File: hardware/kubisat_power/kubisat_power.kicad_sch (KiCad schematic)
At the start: 21 parts, among them U1 TPS79601DCQ, U2 INA3221

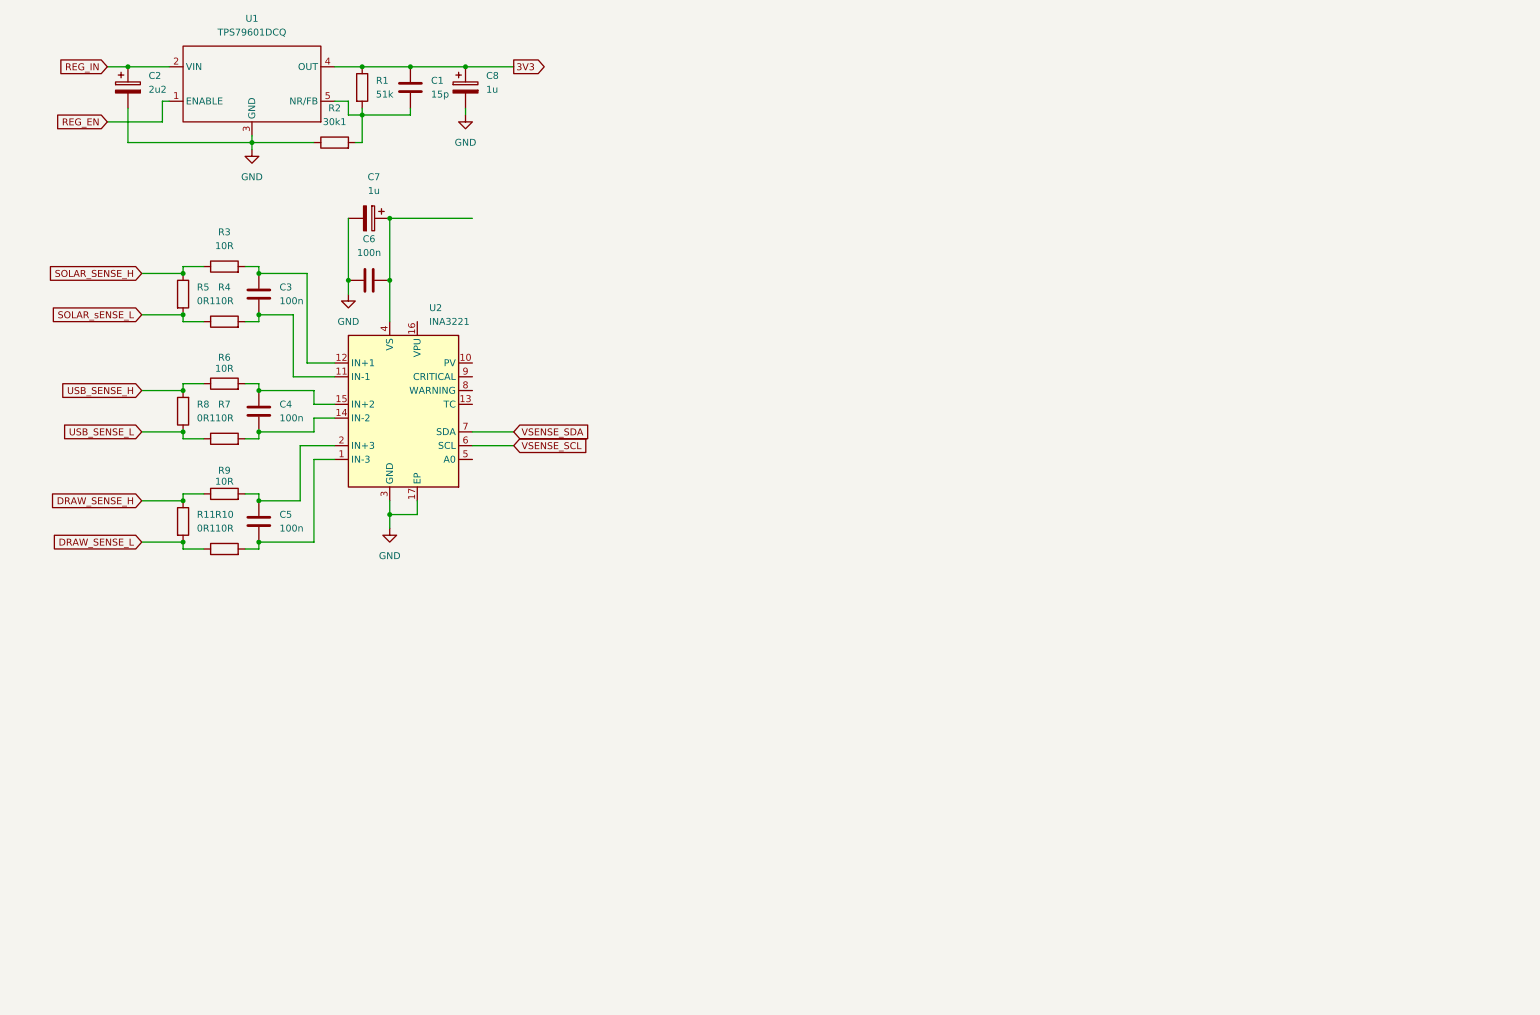
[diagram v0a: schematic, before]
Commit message: complete schematic, todo add solar connectors
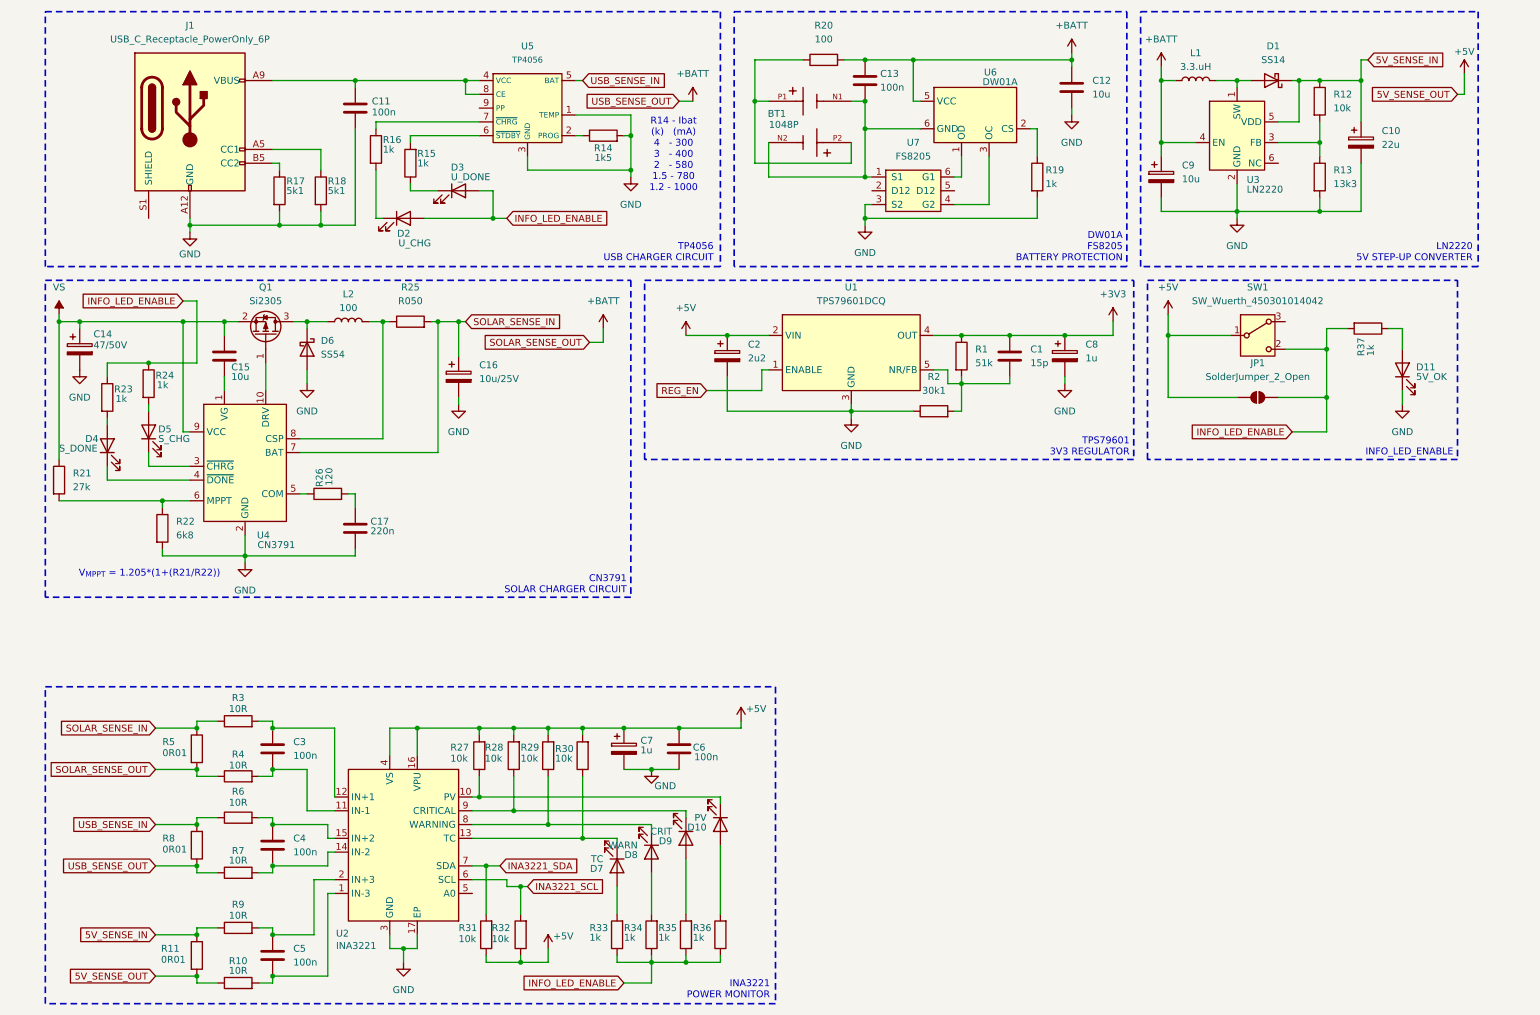
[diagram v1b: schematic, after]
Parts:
- added BT1: 1048P, 1048P:BAT_1048P, symbol 1048P:1048P
- added C10: 22u, Capacitor_SMD:C_1206_3216Metric, symbol Device:C_Polarized
- added C11, C13: 100n, Capacitor_SMD:C_0805_2012Metric, symbol Device:C
- added C12, C15: 10u, Capacitor_SMD:C_0805_2012Metric, symbol Device:C
- added C14: 47/50V, Capacitor_SMD:C_Elec_6.3x5.8, symbol Device:C_Polarized
- added C16: 10u/25V, Capacitor_SMD:C_1210_3225Metric, symbol Device:C_Polarized
- added C17: 220n, Capacitor_SMD:C_0805_2012Metric, symbol Device:C
- added C9: 10u, Capacitor_SMD:C_1206_3216Metric, symbol Device:C_Polarized
- added D1: SS14, Diode_SMD:D_SMA, symbol Device:D_Schottky
- added D10: PV, LED_SMD:LED_0805_2012Metric, symbol Device:LED
- added D11: 5V_OK, LED_SMD:LED_0805_2012Metric, symbol Device:LED
- added D2: U_CHG, LED_SMD:LED_0805_2012Metric, symbol Device:LED
- added D3: U_DONE, LED_SMD:LED_0805_2012Metric, symbol Device:LED
- added D4: S_DONE, LED_SMD:LED_0805_2012Metric, symbol Device:LED
- added D5: S_CHG, LED_SMD:LED_0805_2012Metric, symbol Device:LED
- added D6: SS54, Diode_SMD:D_SMA, symbol Device:D_Schottky
- added D7: TC, LED_SMD:LED_0805_2012Metric, symbol Device:LED
- added D8: WARN, LED_SMD:LED_0805_2012Metric, symbol Device:LED
- added D9: CRIT, LED_SMD:LED_0805_2012Metric, symbol Device:LED
- added J1: USB_C_Receptacle_PowerOnly_6P, Connector_USB:USB_C_Receptacle_HRO_TYPE-C-31-M-17, symbol Connector:USB_C_Receptacle_PowerOnly_6P
- added JP1: SolderJumper_2_Open, Jumper:SolderJumper-2_P1.3mm_Open_RoundedPad1.0x1.5mm, symbol Jumper:SolderJumper_2_Open
- added L1: 3.3.uH, Inductor_SMD:L_Cenker_CKCS5040, symbol Device:L
- added L2: 100, Inductor_SMD:L_Bourns_SRP7028A_7.3x6.6mm, symbol Device:L
- added Q1: Si2305, Package_TO_SOT_SMD:SOT-23, symbol Transistor_FET:Si2319CDS
- added R12, R27, R28, R29, R30, R31, R32: 10k, Resistor_SMD:R_0805_2012Metric, symbol Device:R
- added R13: 13k3, Resistor_SMD:R_0805_2012Metric, symbol Device:R
- added R14: 1k5, Resistor_SMD:R_0805_2012Metric, symbol Device:R
- added R15, R16, R23, R24, R33, R34, R35, R36, R37: 1k, Resistor_SMD:R_0805_2012Metric, symbol Device:R
- added R17, R18: 5k1, Resistor_SMD:R_0805_2012Metric, symbol Device:R
- added R19: 1k, Resistor_SMD:R_2512_6332Metric_Pad1.40x3.35mm_HandSolder, symbol Device:R
- added R20: 100, Resistor_SMD:R_2512_6332Metric_Pad1.40x3.35mm_HandSolder, symbol Device:R
- added R21: 27k, Resistor_SMD:R_0805_2012Metric, symbol Device:R
- added R22: 6k8, Resistor_SMD:R_0805_2012Metric, symbol Device:R
- added R25: R050, Resistor_SMD:R_2512_6332Metric_Pad1.40x3.35mm_HandSolder, symbol Device:R
- added R26: 120, Resistor_SMD:R_0805_2012Metric, symbol Device:R
- added SW1: SW_Wuerth_450301014042, Button_Switch_THT:SW_Slide-03_Wuerth-WS-SLTV_10x2.5x6.4_P2.54mm, symbol Switch:SW_Wuerth_450301014042
- added U3: LN2220, Package_TO_SOT_SMD:TSOT-23-6_HandSoldering, symbol kubisat:LN2220
- added U4: CN3791, Package_SO:SSOP-10-1EP_3.9x4.9mm_P1mm_EP2.1x3.3mm, symbol kubisat:CN3791
- added U5: TP4056, Package_SO:SOIC-8-1EP_3.9x4.9mm_P1.27mm_EP2.29x3mm, symbol kubisat:TP4056
- added U6: DW01A, Package_TO_SOT_SMD:SOT-23-6, symbol Battery_Management:DW01A
- added U7: FS8205, Package_TO_SOT_SMD:SOT-23-6, symbol PCM_marbastlib-various:FS8205
- R11, R5, R8: value 0R1 -> 0R01
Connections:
- net DRAW_SENSE_L is gone; now on net +5V: R10.1, R11.2
- net REG_IN is gone; now on net +5V: C2.1, U1.2 (VIN)
- net USB_SENSE_L is gone; now on net +BATT: R7.1, R8.1
- net GND: now also C6.2, C10.2, C11.2, C12.2, C14.2, C16.2, C17.2, C9.2, D11.1 (K), D6.2 (A), J1.A12 (GND), J1.B12 (GND), R13.2, R14.2, R17.2, R18.2, R19.2, R22.2, U3.2 (GND), U4.2 (GND), U5.1 (TEMP), U5.3 (GND), U7.3 (S2); no longer C6.1
- net +5V: now reaches C7.1, U2.4 (VS)
- net +5V: now also C6.1, U2.16 (VPU), JP1.1 (A), R27.2, R28.2, R29.2, R30.2, R31.1, R32.1, SW1.1 (B); no longer C6.2
- net at U2.10 (PV): now also D10.1 (K), R27.1
- net at U2.13 (TC): now also D7.1 (K), R30.1
- net at U2.8 (WARNING): now also D8.1 (K), R29.1
- net at U2.9 (CRITICAL): now also D9.1 (K), R28.1
- net 3V3 renamed +3V3
- net DRAW_SENSE_H renamed 5V_SENSE_IN
- net 5V_SENSE_IN: now also C10.1, D1.1 (K), R12.1, U3.5 (VDD)
- net SOLAR_SENSE_H renamed SOLAR_SENSE_IN
- net SOLAR_SENSE_IN: now also C16.1, R25.2, U4.7 (BAT)
- net SOLAR_sENSE_L renamed +BATT
- net +BATT: now also C12.1, C13.1, C9.1, L1.1, R20.2, U3.4 (EN), U6.5 (VCC)
- net USB_SENSE_H renamed USB_SENSE_IN
- net USB_SENSE_IN: now also U5.5 (BAT)
- net VSENSE_SCL renamed INA3221_SCL
- net INA3221_SCL: now also R32.2
- net VSENSE_SDA renamed INA3221_SDA
- net INA3221_SDA: now also R31.2
- new net: R12.2, R13.1, U3.3 (FB)
- new net: D4.2 (A), R23.2
- new net: D8.2 (A), R34.2
- new net: D6.1 (K), L2.1, Q1.3 (D)
- new net: L2.2, R25.1, U4.8 (CSP)
- new net: R21.2, R22.1, U4.6 (MPPT)
- new net: D5.2 (A), R24.2
- new net: Q1.1 (G), U4.10 (DRV)
- new net: D4.1 (K), U4.4 (~{DONE})
- new net: D3.1 (K), R15.1
- new net: BT1.N1, BT1.N2, C13.2, U6.6 (GND), U7.1 (S1)
- new net: BT1.P1, BT1.P2, R20.1
- new net: C15.2, U4.1 (VG)
- new net: D5.1 (K), U4.3 (~{CHRG})
- new net: R26.1, U4.5 (COM)
- new net: U6.1 (OD), U7.6 (G1)
- new net: R19.1, U6.2 (CS)
- new net: U6.3 (OC), U7.4 (G2)
- new net: R14.1, U5.2 (PROG)
- new net: C11.1, J1.A9 (VBUS), J1.B9 (VBUS), U5.4 (VCC), U5.8 (CE)
- new net: R15.2, U5.6 (~{STDBY})
- new net: R16.1, U5.7 (~{CHRG})
- new net: D10.2 (A), R36.2
- new net: D7.2 (A), R33.2
- new net: D2.1 (K), R16.2
- new net: D9.2 (A), R35.2
- new net: C17.1, R26.2
- new net: D1.2 (A), L1.2, U3.1 (SW)
- new net: J1.B5 (CC2), R17.1
- new net: D11.2 (A), R37.1
- new net: J1.A5 (CC1), R18.1
- new net INFO_LED_ENABLE: D2.2 (A), D3.2 (A), JP1.2 (B), R23.1, R24.1, R33.1, R34.1, R35.1, R36.1, R37.2, SW1.2 (C)
- new net VS: C14.1, C15.1, Q1.2 (S), R21.1, U4.9 (VCC)
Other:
- note added: "CN3791 SOLAR CHARGER CIRCUIT"
- note added: "DW01A FS8205 BATTERY PROTECTION"
- note added: "INA3221 POWER MONITOR"
- note added: "INFO_LED_ENABLE"
- note added: "LN2220 5V STEP-UP CONVERTER"
- note added: "R14 - Ibat (k) (mA) 4 - 300 3 - 400 2 - 580 1.5 - 780 1.2 - 1000"
- note added: "TP4056 USB CHARGER CIRCUIT"
- note added: "TPS79601 3V3 REGULATOR"
- note added: "V_{MPPT} = 1.205*(1+(R21/R22))"
- moved on the sheet: C1, C2, C3, C4, C5, C6, C7, C8, R1, R10, R11, R2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

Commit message: complete schematic, todo add solar connectors
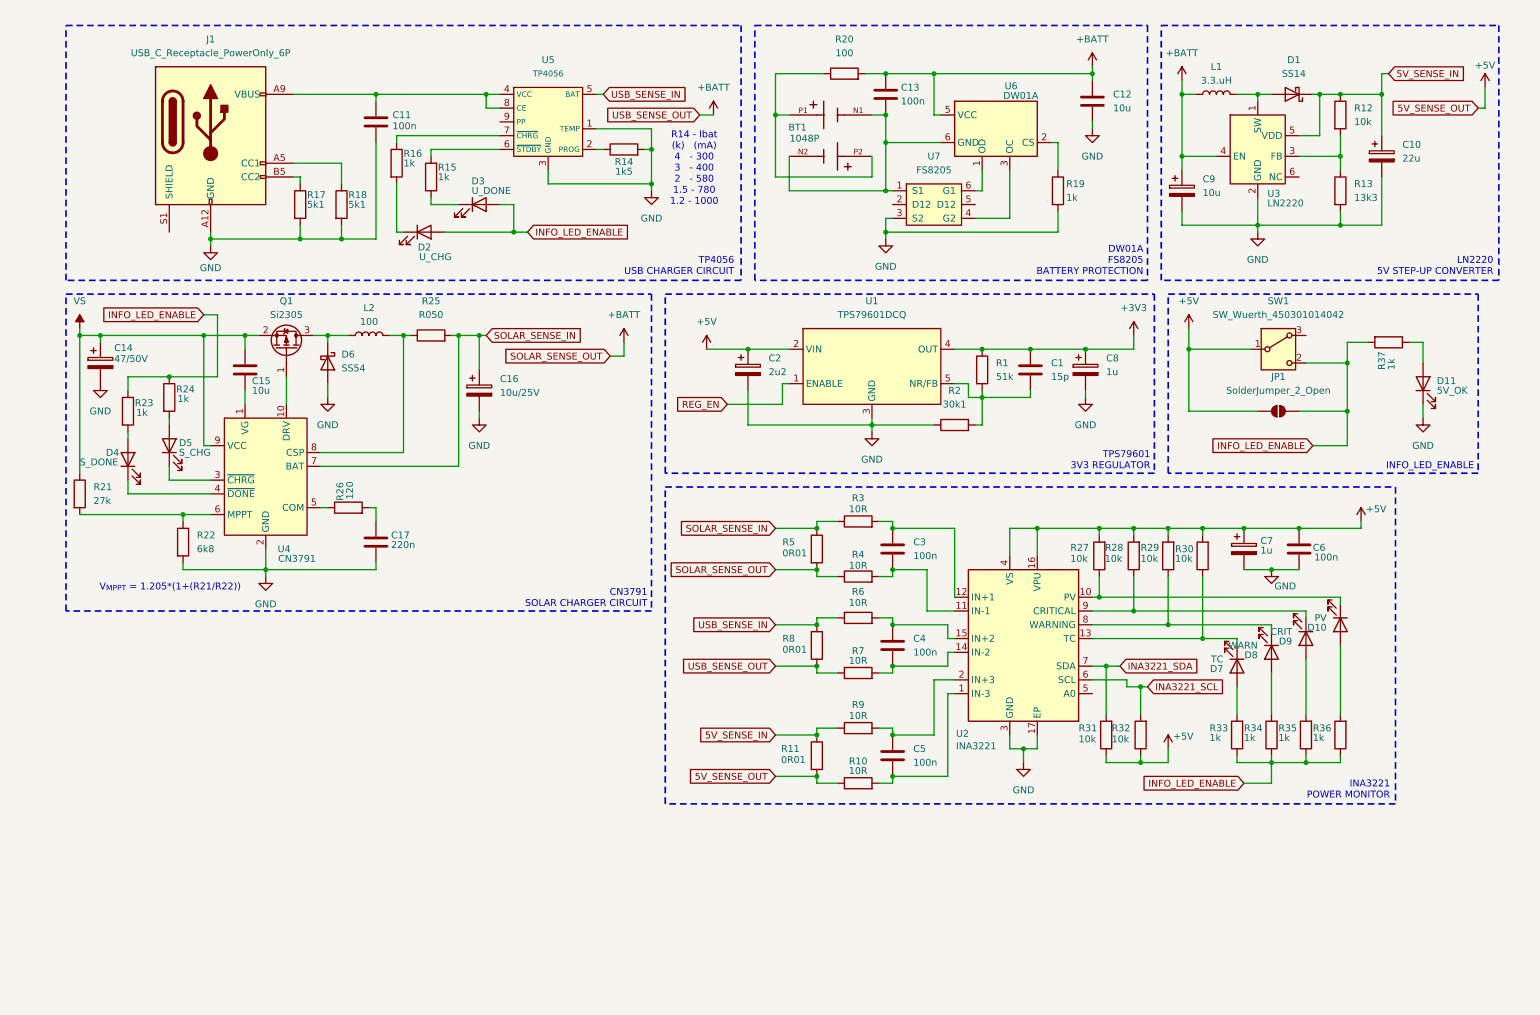
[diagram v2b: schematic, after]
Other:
- moved on the sheet: BT1, C1, C10, C11, C12, C13, C14, C15, C16, C17, C2, C3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
